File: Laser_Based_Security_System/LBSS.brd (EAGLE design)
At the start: 114.3 x 49.5 mm, 23 parts, among them IC1 7805TV

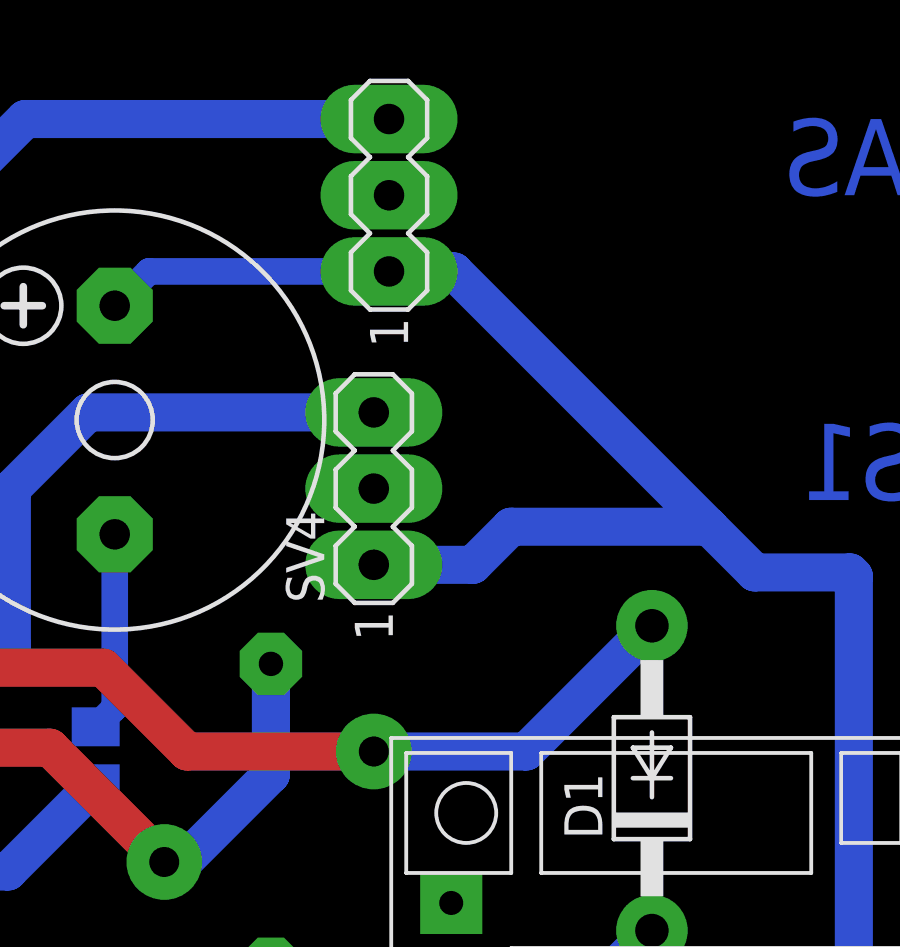
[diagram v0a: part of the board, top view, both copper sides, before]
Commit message: Added Schematic
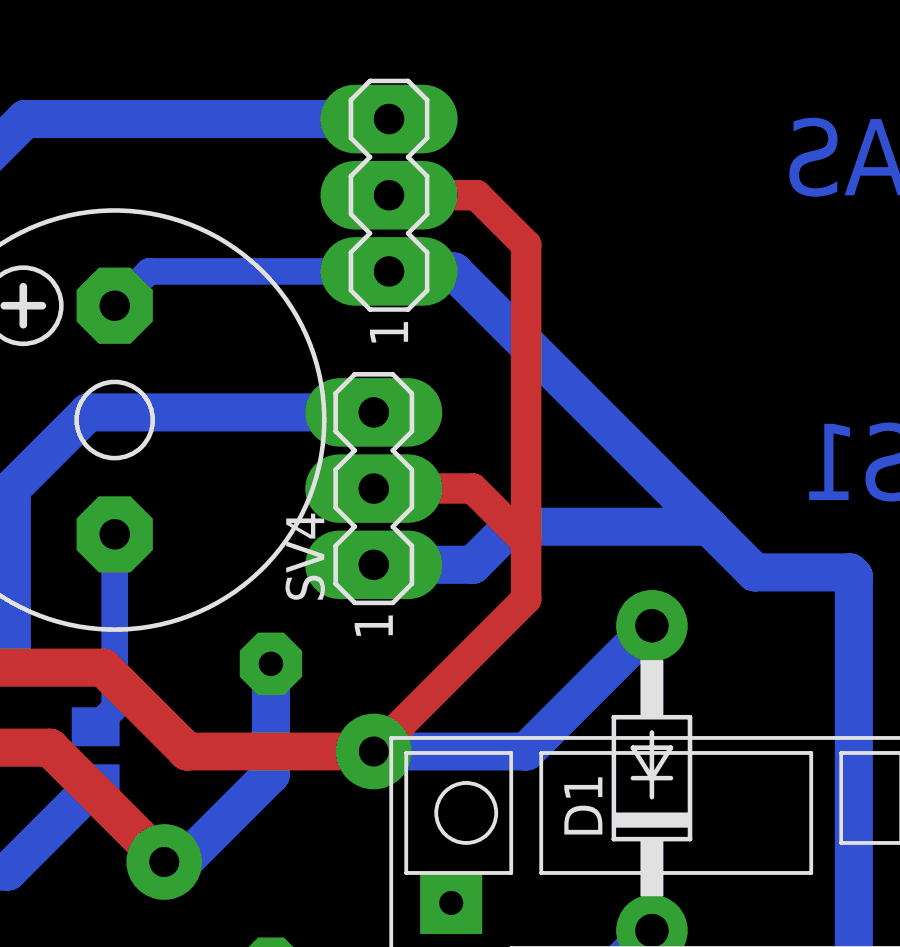
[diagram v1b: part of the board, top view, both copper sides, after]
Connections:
- net 5V: now also SV2.2, SV4.2
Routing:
- net 5V: track 147.2 -> 177.3 mm
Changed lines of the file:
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@@
 <wire x1="38.1" y1="26.289" x2="38.1" y2="20.955" width="1.27" layer="16"/>
 <wire x1="38.1" y1="29.21" x2="38.1" y2="34.29" width="0.889" layer="16"/>
+<contactref element="SV2" pad="2"/>
+<contactref element="SV4" pad="2"/>
+<wire x1="85.979" y1="23.749" x2="91.059" y2="28.829" width="1.016" layer="1"/>
+<wire x1="91.059" y1="28.829" x2="91.059" y2="30.734" width="1.016" layer="1"/>
+<wire x1="91.059" y1="30.734" x2="89.281" y2="32.512" width="1.016" layer="1"/>
+<wire x1="89.281" y1="32.512" x2="85.979" y2="32.512" width="1.016" layer="1"/>
+<wire x1="91.059" y1="30.734" x2="91.059" y2="40.64" width="1.016" layer="1"/>
+<wire x1="89.408" y1="42.291" x2="86.487" y2="42.291" width="1.016" layer="1"/>
+<wire x1="91.059" y1="40.64" x2="89.408" y2="42.291" width="1.016" layer="1"/>
 </signal>
 <signal name="A7">
